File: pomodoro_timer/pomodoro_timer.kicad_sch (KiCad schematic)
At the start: 37 parts, among them J1 UPDI Flash Header, J2 I2C Header, P1 Conn_USB_A_Plain, Q1 MOSFET SOT23, SW1 Start/Stop, SW2 Skip, SW3 Restart, U1 ATtiny412, U10 WS2812B, U11 WS2812B, U12 WS2812B, U13 WS2812B, U14 Lin Reg 3.3V 1A, U2 WS2812B, U3 WS2812B, U4 WS2812B, U5 WS2812B, U6 WS2812B, U7 WS2812B, U8 WS2812B, U9 WS2812B

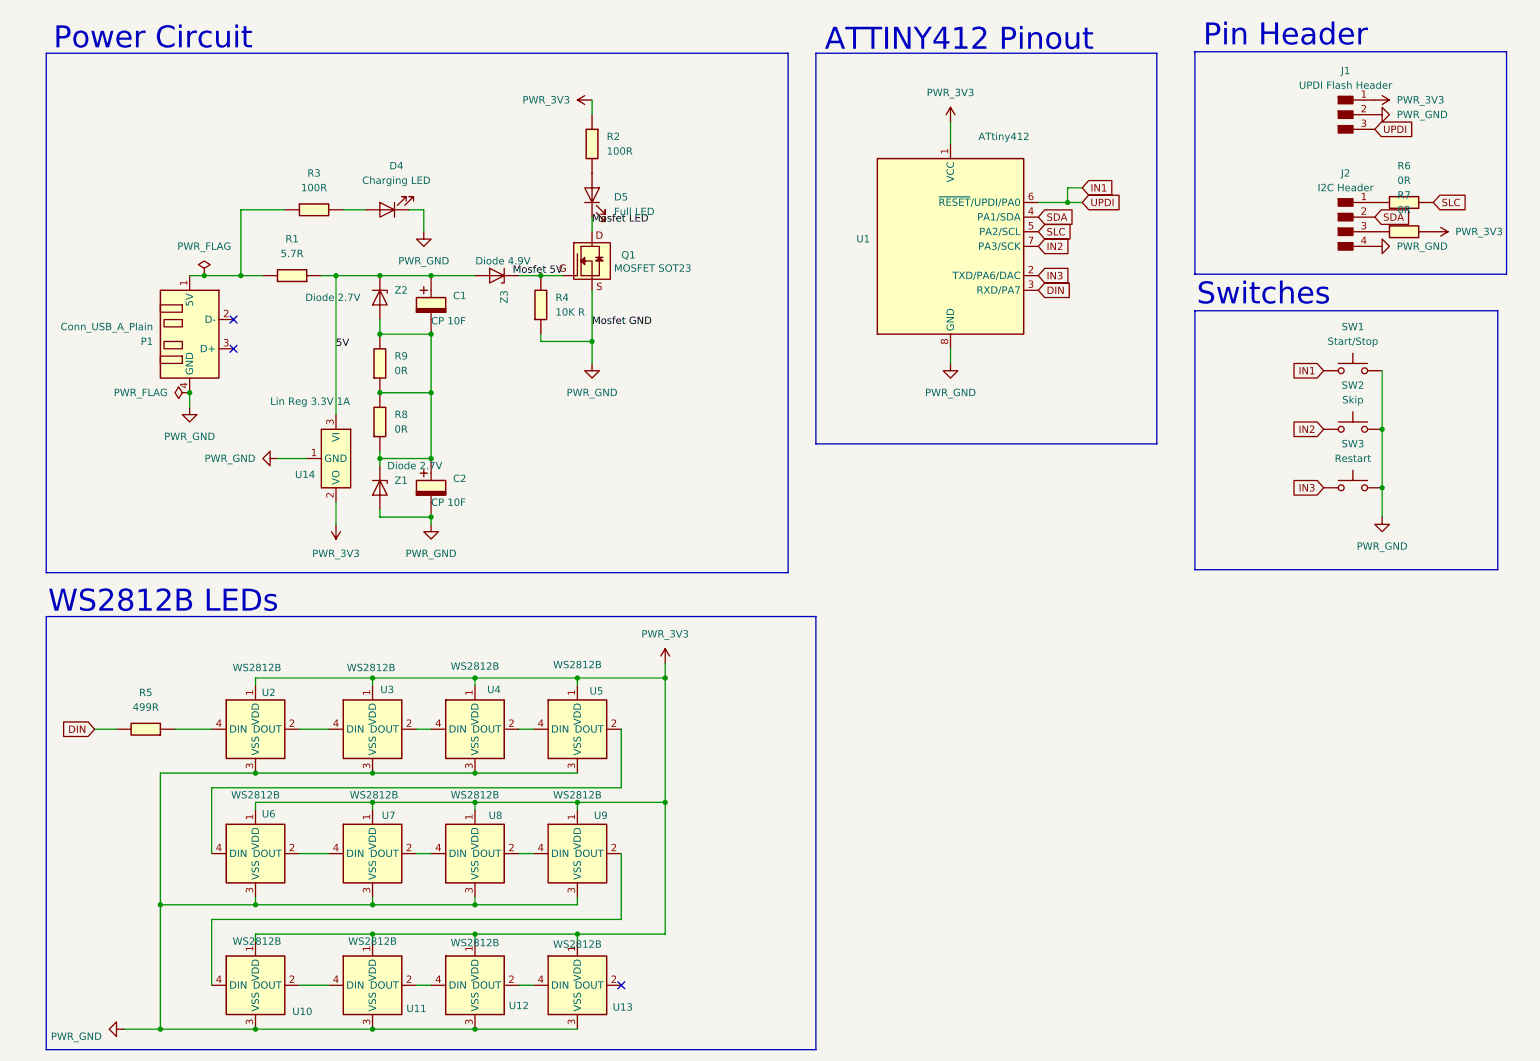
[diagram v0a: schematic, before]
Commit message: PCB: updated schematics and routing
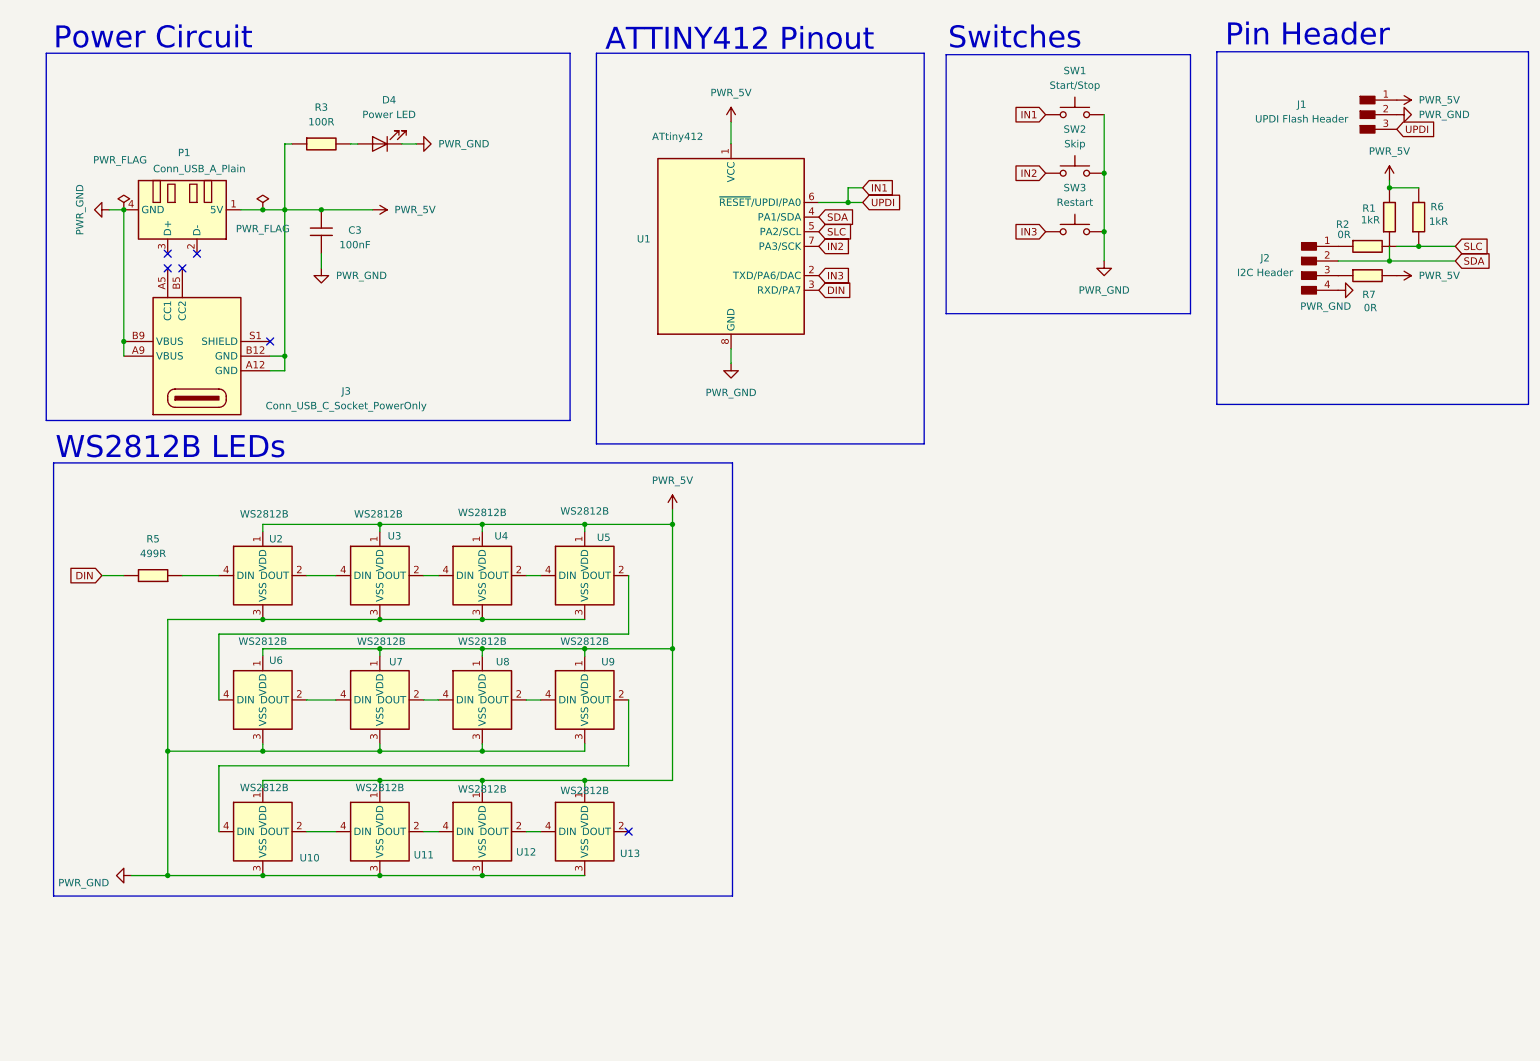
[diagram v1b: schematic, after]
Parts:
- removed C1, C2: CP 10F, fab:CP_Elec_10F_Tecate_TPLC-3R8, symbol fab:CP_Elec_10F_Tecate_TPLC-3R8
- removed D5: Full LED, fab:LED_1206, symbol fab:LED_1206
- removed Q1: MOSFET SOT23, fab:SOT-23-3, symbol fab:Transistor_MOSFET_NCh_SOT23
- removed R4: 10K R, fab:R_1206, symbol fab:R_1206
- removed R8, R9: 0R, fab:R_1206, symbol fab:R_1206
- removed U14: Lin Reg 3.3V 1A, fab:SOT-223-3_TabPin2, symbol fab:Regulator_Linear_3.3V_1A_DiodesIncorporated
- removed Z1, Z2: Diode 2.7V, fab:SOD-123, symbol fab:Diode_Zener_SOD123
- removed Z3: Diode 4.9V, fab:SOD-123, symbol fab:Diode_Zener_SOD123
- added C3: 100nF, fab:C_1206, symbol fab:C_1206
- added J3: Conn_USB_C_Socket_PowerOnly, fab:Conn_USB_C_Socket_GCT_USB4125-GF-A-0190, symbol fab:Conn_USB_C_Socket_PowerOnly
- D4: value Charging LED -> Power LED
- R1: value 5.7R -> 1kR
- R2: value 100R -> 0R
- R6: value 0R -> 1kR
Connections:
- net 5V is gone; now on net SDA: R1.2
- net PWR_GND: now also C3.2, J3.A9 (VBUS), J3.B9 (VBUS)
- net SLC: now also R2.1, R6.2; no longer R6.1
- net PWR_5V: now reaches P1.1 (5V), R1.1, R3.2
- net PWR_5V: now also J1.1 (Pin_1), R6.1, R7.1, U1.1 (VCC), U10.1 (VDD), U11.1 (VDD), U12.1 (VDD), U13.1 (VDD), U2.1 (VDD), U3.1 (VDD), U4.1 (VDD), U5.1 (VDD), U6.1 (VDD), U7.1 (VDD), U8.1 (VDD), U9.1 (VDD), C3.1, J3.A12 (GND), J3.B12 (GND)
- net at J2.1 (Pin_1): now also R2.2; no longer R6.2
- removed net PWR_3V3: J1.1 (Pin_1), R2.2, R7.1, U1.1 (VCC), U10.1 (VDD), U11.1 (VDD), U12.1 (VDD), U13.1 (VDD), U2.1 (VDD), U3.1 (VDD), U4.1 (VDD), U5.1 (VDD), U6.1 (VDD), U7.1 (VDD), U8.1 (VDD), U9.1 (VDD)
- no-connect marks 3 -> 6
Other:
- moved on the sheet: D4, J1, J2, P1, R3, R5, R6, R7, SW1, SW2, SW3, U1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
